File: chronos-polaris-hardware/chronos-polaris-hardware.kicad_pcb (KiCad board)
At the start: 2 copper layers, 30 x 50 mm, 61 parts, among them J1 Conn_01x03_Pin, J2 Conn_01x03_Pin, J3 Conn_01x03_Pin, J4 Conn_01x03_Pin, J5 Conn_01x03_Pin, J6 Conn_01x04, J7 Conn_01x04, J8 Conn_01x02, P1 WJ124-3_81-6P, U1 TPS62172DSGR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

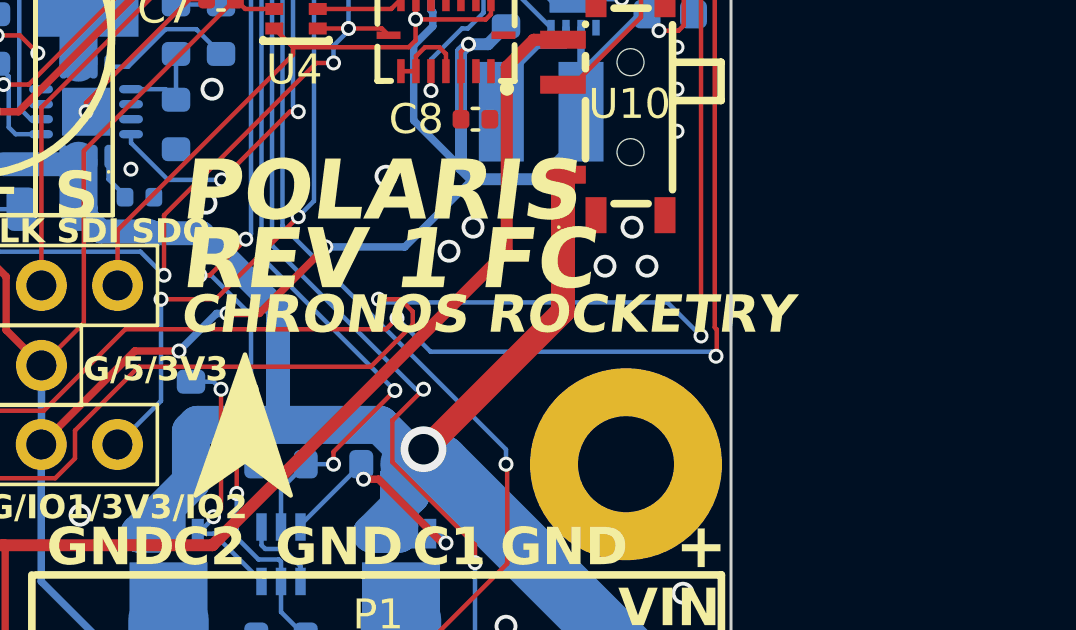
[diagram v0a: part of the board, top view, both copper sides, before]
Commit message: Improve orientation tracking; add servo support, fake TVC
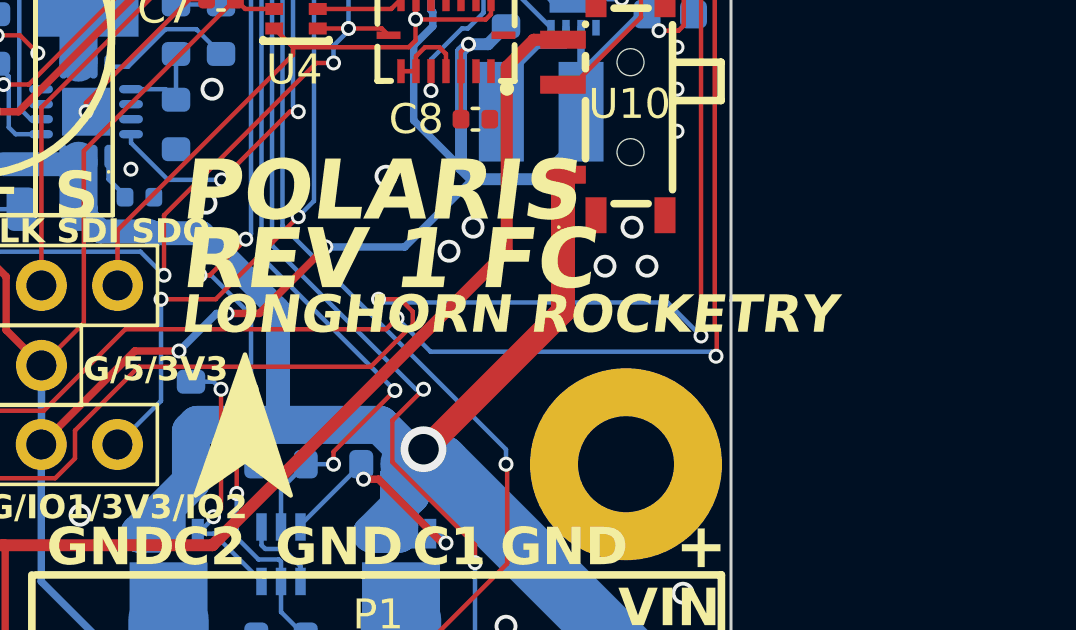
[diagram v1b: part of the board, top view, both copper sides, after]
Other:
- board text added: "LONGHORN ROCKETRY"
